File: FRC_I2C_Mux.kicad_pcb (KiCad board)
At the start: 2 copper layers, 47.2 x 44.2 mm, 48 parts, among them J1 Conn_01x04, J10 Conn_01x04, J11 Conn_01x04, J12 Conn_01x02, J2 Conn_01x04, J3 Conn_01x04, J4 Conn_01x04, J5 Conn_01x04, J6 Conn_01x02, J7 Conn_01x02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

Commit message: Remap footprints and update gitignore
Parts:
- C1: footprint Capacitor_SMD:C_0805_2012Metric_Pad1.18x1.45mm_HandSolder -> footprints:C_0805_2012Metric_Pad1.18x1.45mm_HandSolder
- D1: footprint SamacSys_Parts:LEDC1006X25N -> footprints:LEDC1006X25N
- G***: footprint Bitmaps:canman_soldermask -> footprints:canman_soldermask
- G***: footprint Bitmaps:canman_copper -> footprints:canman_copper
- J1, J10, J11, J2, J3, J4, J5, J8, J9: footprint Connector_PinHeader_2.54mm:PinHeader_1x04_P2.54mm_Vertical -> footprints:PinHeader_1x04_P2.54mm_Vertical
- J12, J6, J7: footprint Connector_PinHeader_2.54mm:PinHeader_1x02_P2.54mm_Vertical -> footprints:PinHeader_1x02_P2.54mm_Vertical
- R1, R10, R11, R12, R13, R14, R15, R16, R17, R18, R19, R2, R20, R21, R22, R23, R24, R3, R4, R5, R6, R7, R8, R9: footprint Resistor_SMD:R_0402_1005Metric_Pad0.72x0.64mm_HandSolder -> footprints:R_0402_1005Metric_Pad0.72x0.64mm_HandSolder
- REF1, REF2, REF3, REF4: footprint MountingHole:MountingHole_2.5mm_Pad_Via -> footprints:MountingHole_2.5mm_Pad_Via
- RN1, RN2: footprint SamacSys_Parts:EXB2HV_1 -> footprints:EXB2HV_1
- SW1: footprint Button_Switch_SMD:SW_SPST_SKQG_WithStem -> footprints:SW_SPST_SKQG_WithStem
- U1: footprint Package_SO:SOIC-24W_7.5x15.4mm_P1.27mm -> footprints:SOIC-24W_7.5x15.4mm_P1.27mm

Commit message: Fix footprint paths
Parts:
- C1: footprint footprints:C_0805_2012Metric_Pad1.18x1.45mm_HandSolder -> Capacitor_SMD:C_0805_2012Metric_Pad1.18x1.45mm_HandSolder
- J1, J10, J11, J2, J3, J4, J5, J8, J9: footprint footprints:PinHeader_1x04_P2.54mm_Vertical -> Connector_PinHeader_2.54mm:PinHeader_1x04_P2.54mm_Vertical
- J12, J6, J7: footprint footprints:PinHeader_1x02_P2.54mm_Vertical -> Connector_PinHeader_2.54mm:PinHeader_1x02_P2.54mm_Vertical
- R1, R10, R11, R12, R13, R14, R15, R16, R17, R18, R19, R2, R20, R21, R22, R23, R24, R3, R4, R5, R6, R7, R8, R9: footprint footprints:R_0402_1005Metric_Pad0.72x0.64mm_HandSolder -> Resistor_SMD:R_0402_1005Metric_Pad0.72x0.64mm_HandSolder
- REF1, REF2, REF3, REF4: footprint footprints:MountingHole_2.5mm_Pad_Via -> MountingHole:MountingHole_2.5mm_Pad_Via
- SW1: footprint footprints:SW_SPST_SKQG_WithStem -> Button_Switch_SMD:SW_SPST_SKQG_WithStem
- U1: footprint footprints:SOIC-24W_7.5x15.4mm_P1.27mm -> Package_SO:SOIC-24W_7.5x15.4mm_P1.27mm

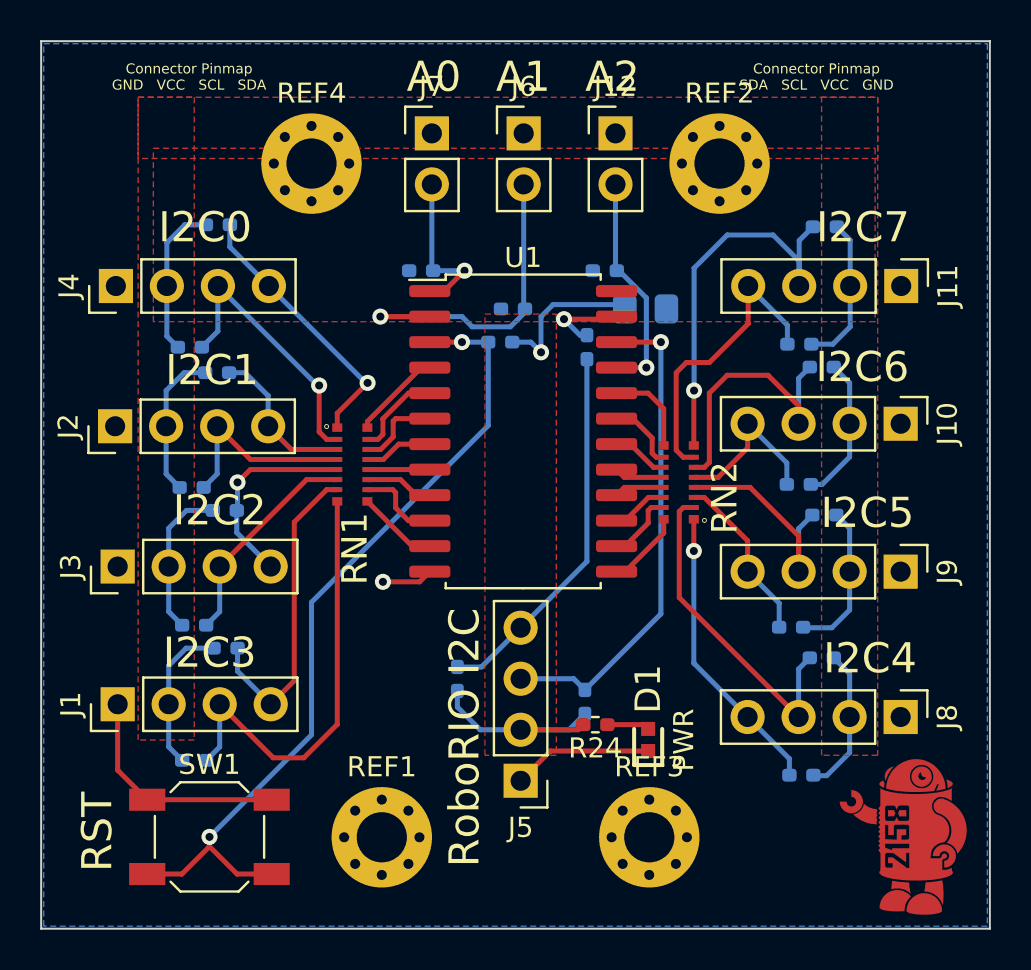
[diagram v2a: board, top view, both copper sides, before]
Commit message: Update resistors to 0805s
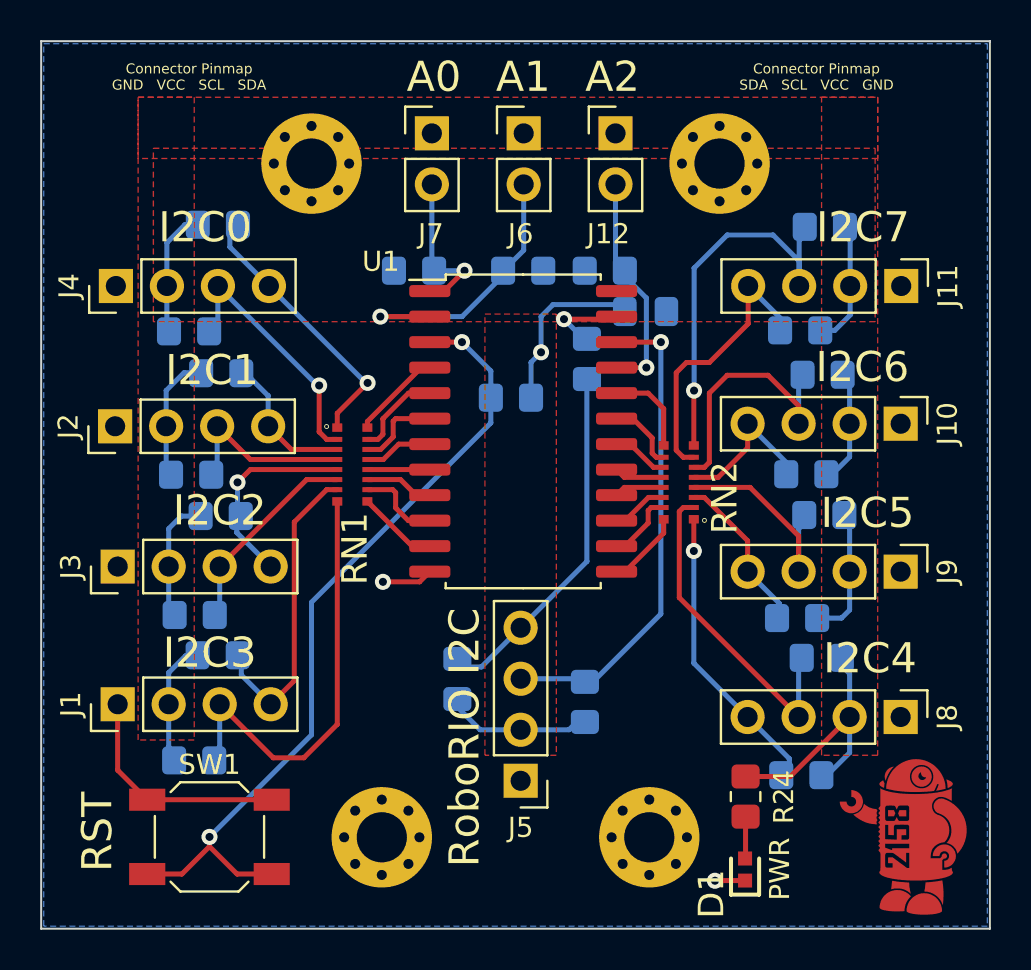
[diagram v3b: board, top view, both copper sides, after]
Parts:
- R1, R10, R11, R12, R13, R14, R15, R16, R17, R18, R19, R2, R20, R21, R22, R23, R24, R3, R4, R5, R6, R7, R8, R9: footprint Resistor_SMD:R_0402_1005Metric_Pad0.72x0.64mm_HandSolder -> Resistor_SMD:R_0805_2012Metric_Pad1.20x1.40mm_HandSolder
- moved R24 8.29 mm to (148.6, 92.0), turned to 90 degrees
- moved D1 8.06 mm to (148.6, 95.6)
- moved R20 2.82 mm to (136.9, 72.1)
- moved R21 1.97 mm to (137.5, 65.8), turned to 0 degrees
- moved R18 0.79 mm to (120.9, 68.8)
- moved R4 0.69 mm to (151.3, 68.8)
- moved R15 0.64 mm to (121.0, 75.9)
- moved R8 0.63 mm to (151.6, 75.9)
- moved R9 0.58 mm to (140.7, 70.2)
- moved R5 0.54 mm to (151.2, 83.1)
- moved R13 0.53 mm to (122.3, 84.9)
- moved R17 0.51 mm to (121.2, 82.9)
- moved R6 0.38 mm to (152.5, 71.0)
- moved R22 0.36 mm to (132.1, 65.8)
- moved R19 0.35 mm to (122.5, 78.0)
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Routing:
- net +3V3: track 79.4 -> 73.9 mm
- net GND: track 21.1 -> 15.6 mm, vias 1 -> 2
- net /A1: track 16.6 -> 14.4 mm
- net /SCL0: track 13.8 -> 12.7 mm
- net /SCL2: track 10.8 -> 9.90 mm
- net /SCL1: track 9.99 -> 9.04 mm
- net /SDA7: track 15.1 -> 14.2 mm
- net /SCL6: track 13.7 -> 12.9 mm
- net /SDA: track 18.7 -> 18.0 mm
- net Net-(R20-Pad2): track 41.1 -> 40.5 mm
- net /SDA1: track 7.86 -> 7.24 mm

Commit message: Replace LED with 0805
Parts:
- D1: footprint footprints:LEDC1006X25N -> LED_SMD:LED_0805_2012Metric_Pad1.15x1.40mm_HandSolder
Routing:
- net GND: track 15.6 -> 17.6 mm
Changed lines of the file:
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@@
     )
   )
-  (footprint "footprints:LEDC1006X25N" (layer "F.Cu")
+  (footprint "LED_SMD:LED_0805_2012Metric_Pad1.15x1.40mm_HandSolder" (layer "F.Cu")
     (at 148.59 95.6056 90)
-    (descr "SML-P11MTT86")
-    (tags "LED")
+    (descr "LED SMD 0805 (2012 Metric), square (rectangular) end terminal, IPC_7351 nominal, (Body size source: https://docs.google.com/spreadsheets/d/1BsfQQcO9C6DZCsRaXUlFlo91Tg2WpOkGARC1WS5S8t0/edit?usp=sharing), generated with kicad-footprint-generator")
+    (tags "LED handsolder")
     (property "Sheetfile" "FRC_I2C_Mux.kicad_sch")
     (property "Sheetname" "")
     (attr smd)
-    (fp_text reference "D1" (at -1.2192 -1.6764 90) (layer "F.SilkS")
-      (effects (font (size 1.27 1.27) (thickness 0.254)))
+    (fp_text reference "D1" (at 0 -1.65 90) (layer "F.SilkS")
+      (effects (font (size 1 1) (thickness 0.15)))
     )
-    (fp_text value "LED" (at 0 0 90) (layer "F.SilkS") hide
-      (effects (font (size 1.27 1.27) (thickness 0.254)))
+    (fp_text value "LED" (at 0 1.65 90) (layer "F.Fab")
+      (effects (font (size 1 1) (thickness 0.15)))
     )
     (fp_text user "${REFERENCE}" (at 0 0 90) (layer "F.Fab")
-      (effects (font (size 1.27 1.27) (thickness 0.254)))
+      (effects (font (size 0.5 0.5) (thickness 0.08)))
     )
-    (fp_line (start -1.25 0.7) (end 0.55 0.7) (layer "F.SilkS") (width 0.2))
-    (fp_line (start 0.55 -0.7) (end -1.25 -0.7) (layer "F.SilkS") (width 0.2))
-    (fp_line (start -1.25 -0.7) (end -1.25 0.7) (layer "F.SilkS") (width 0.2))
-    (fp_line (start 1.35 -0.8) (end 1.35 0.8) (layer "F.CrtYd") (width 0.05))
-    (fp_line (start -1.35 -0.8) (end 1.35 -0.8) (layer "F.CrtYd") (width 0.05))
-    (fp_line (start 1.35 0.8) (end -1.35 0.8) (layer "F.CrtYd") (width 0.05))
-    (fp_line (start -1.35 0.8) (end -1.35 -0.8) (layer "F.CrtYd") (width 0.05))
-    (fp_line (start -0.5 -0.3) (end 0.5 -0.3) (layer "F.Fab") (width 0.1))
-    (fp_line (start 0.5 -0.3) (end 0.5 0.3) (layer "F.Fab") (width 0.1))
-    (fp_line (start 0.5 0.3) (end -0.5 0.3) (layer "F.Fab") (width 0.1))
-    (fp_line (start -0.5 0.3) (end -0.5 -0.3) (layer "F.Fab") (width 0.1))
-    (fp_line (start -0.5 -0.1) (end -0.3 -0.3) (layer "F.Fab") (width 0.1))
-    (pad "1" smd rect locked (at -0.55 0 180) (size 0.7 0.7) (layers "F.Cu" "F.Paste" "F.Mask")
+    (fp_line (start -1.86 -0.96) (end -1.86 0.96) (layer "F.SilkS") (width 0.12))
+    (fp_line (start 1 -0.96) (end -1.86 -0.96) (layer "F.SilkS") (width 0.12))
+    (fp_line (start -1.86 0.96) (end 1 0.96) (layer "F.SilkS") (width 0.12))
+    (fp_line (start 1.85 0.95) (end -1.85 0.95) (layer "F.CrtYd") (width 0.05))
+    (fp_line (start -1.85 -0.95) (end 1.85 -0.95) (layer "F.CrtYd") (width 0.05))
+    (fp_line (start 1.85 -0.95) (end 1.85 0.95) (layer "F.CrtYd") (width 0.05))
+    (fp_line (start -1.85 0.95) (end -1.85 -0.95) (layer "F.CrtYd") (width 0.05))
+    (fp_line (start -1 -0.3) (end -1 0.6) (layer "F.Fab") (width 0.1))
+    (fp_line (start 1 -0.6) (end -0.7 -0.6) (layer "F.Fab") (width 0.1))
+    (fp_line (start 1 0.6) (end 1 -0.6) (layer "F.Fab") (width 0.1))
+    (fp_line (start -1 0.6) (end 1 0.6) (layer "F.Fab") (width 0.1))
+    (fp_line (start -0.7 -0.6) (end -1 -0.3) (layer "F.Fab") (width 0.1))
+    (pad "1" smd roundrect (at -1.025 0 90) (size 1.15 1.4) (layers "F.Cu" "F.Paste" "F.Mask") (roundrect_rratio 0.217391)
       (net 2 "GND") (pinfunction "K") (pintype "passive"))
-    (pad "2" smd rect locked (at 0.55 0 180) (size 0.7 0.7) (layers "F.Cu" "F.Paste" "F.Mask")
+    (pad "2" smd roundrect (at 1.025 0 90) (size 1.15 1.4) (layers "F.Cu" "F.Paste" "F.Mask") (roundrect_rratio 0.217391)
       (net 42 "Net-(D1-Pad2)") (pinfunction "A") (pintype "passive"))
-    (model "C:\\Users\\azvan\\Documents\\KiCad\\6.0\\SamacSys_Parts.3dshapes\\SML-P11MTT86R.stp"
-      (offset (xyz -0.02999999888 0 0.09999999999))
+    (model "${KICAD6_3DMODEL_DIR}/LED_SMD.3dshapes/LED_0805_2012Metric.wrl"
+      (offset (xyz 0 0 0))
       (scale (xyz 1 1 1))
-      (rotate (xyz -90 0 0))
+      (rotate (xyz 0 0 0))
     )
   )
@@
   (segment (start 153.0075 85.065) (end 153.797 85.8545) (width 0.25) (layer "B.Cu") (net 1))
   (segment (start 120.7262 84.963) (end 121.5042 84.963) (width 0.25) (layer "B.Cu") (net 1))
+  (segment (start 145.3896 97.3328) (end 146.0918 96.6306) (width 0.25) (layer "F.Cu") (net 2))
   (segment (start 118.82 92.13) (end 125.02 92.13) (width 0.25) (layer "F.Cu") (net 2))
-  (segment (start 148.59 96.1556) (end 147.1002 96.1556) (width 0.25) (layer "F.Cu") (net 2))
   (segment (start 132.383 81.28) (end 130.556 81.28) (width 0.25) (layer "F.Cu") (net 2))
   (segment (start 117.348 90.658) (end 118.82 92.13) (width 0.25) (layer "F.Cu") (net 2))
-  (segment (start 147.1002 96.1556) (end 147.0914 96.1644) (width 0.25) (layer "F.Cu") (net 2))
+  (segment (start 146.0918 96.6306) (end 148.59 96.6306) (width 0.25) (layer "F.Cu") (net 2))
   (segment (start 117.348 87.376) (end 117.348 90.658) (width 0.25) (layer "F.Cu") (net 2))
   (segment (start 132.891 80.772) (end 132.383 81.28) (width 0.25) (layer "F.Cu") (net 2))
   (via (at 130.556 81.28) (size 0.8) (drill 0.4) (layers "F.Cu" "B.Cu") (net 2))
-  (via (at 147.0914 96.1644) (size 0.8) (drill 0.4) (layers "F.Cu" "B.Cu") (net 2))
+  (via (at 145.3896 97.3328) (size 0.8) (drill 0.4) (layers "F.Cu" "B.Cu") (net 2))
   (segment (start 132.891 66.802) (end 133.604 66.802) (width 0.25) (layer "F.Cu") (net 3))
   (segment (start 133.604 66.802) (end 134.62 65.786) (width 0.25) (layer "F.Cu") (net 3))

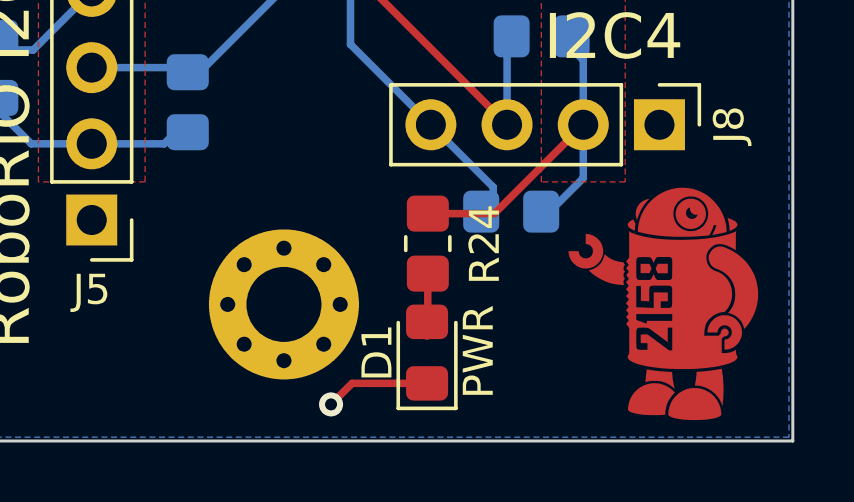
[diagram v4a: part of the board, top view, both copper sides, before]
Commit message: Add mouser links to BoM
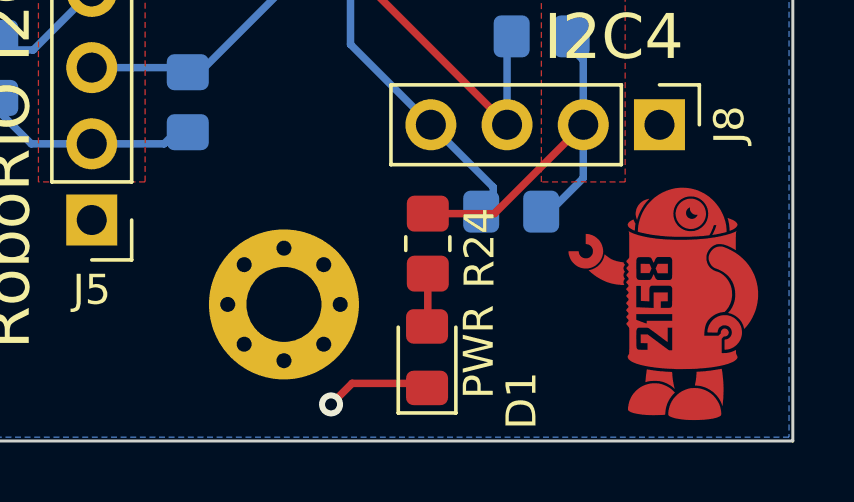
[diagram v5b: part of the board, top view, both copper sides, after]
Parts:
- R24: value 200 -> 33
- moved D1 0.15 mm to (148.6, 95.8)
